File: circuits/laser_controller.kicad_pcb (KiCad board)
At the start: 4 copper layers, 173 x 61.1 mm, 181 parts, among them J1 USB_MINI_B, J2 USB_MINI_B, J5 24V DC IN, J6 CONN_RJ45, J7 C192300, Q1 SOT-23, Q2 SOT-23, Q3 SOT-23, Q4 SOT-23, Q5 SOT-23, Q6 SOT-23, SW1 SW_PUSH, SW2 SW_PUSH, SW3 SW_PUSH, U1 SOIC-8_3.9x4.9mm_P1.27mm, U10 QFN-28-1EP_5x5mm_P0.5mm_EP3.3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, U11 SOT-23-5, U12 TSSOP-14_4.4x5mm_P0.65mm, U13 SOT-23, U14 LQFP-64_10x10mm_P0.5mm, U15 TSOT-23-6, U16 TSOT-23-6, U2 SOIC-8_3.9x4.9mm_P1.27mm, U3 SOIC-8_3.9x4.9mm_P1.27mm, U4 SOIC-8_3.9x4.9mm_P1.27mm, U5 SOT-23-5, U6 SOT-23-5, U7 SOT-23-5, U8 SOT-23-5, U9 ESP32-S3-WROOM-1

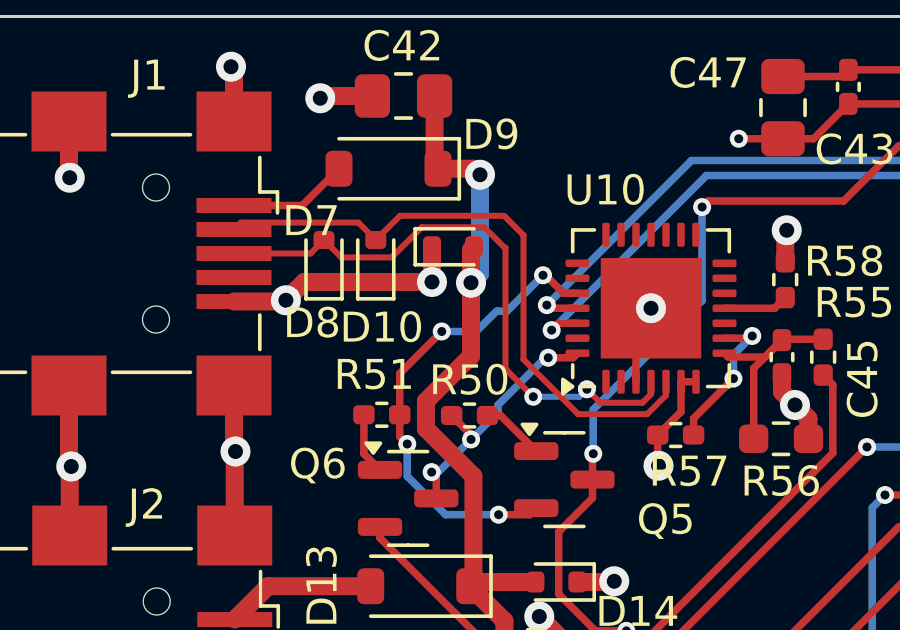
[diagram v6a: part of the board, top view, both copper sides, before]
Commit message: Fix USB PCB routing policy
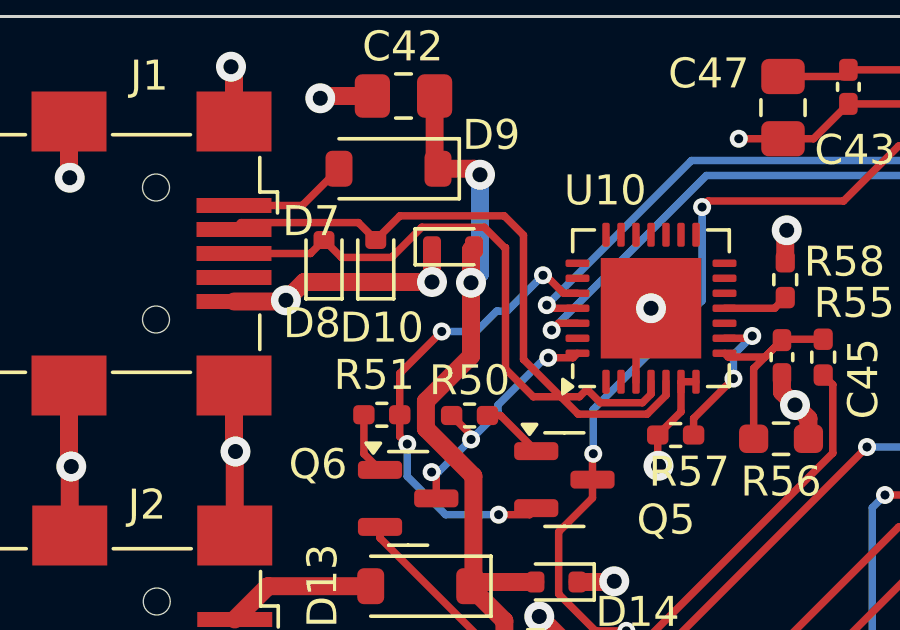
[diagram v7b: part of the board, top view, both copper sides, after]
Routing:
- net /MCU_ESP32-S3/D+: vias 2 -> 0
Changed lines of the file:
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@@
   (segment (start 189.4465 84.434) (end 189.4465 85.962) (width 0.5) (layer "F.Cu") (net 10))
   (segment (start 191.7355 84.434) (end 189.4465 84.434) (width 0.5) (layer "F.Cu") (net 10))
-  (segment (start 51.7389 92.3) (end 52.1889 92.75) (width 0.2) (layer "F.Cu") (net 11))
-  (segment (start 43.555 87.905) (end 45.229448 87.905) (width 0.2) (layer "F.Cu") (net 11))
-  (segment (start 42.975 87.325) (end 43.555 87.905) (width 0.2) (layer "F.Cu") (net 11))
-  (segment (start 49.025 87.580132) (end 49.025 91.625) (width 0.2) (layer "F.Cu") (net 11))
-  (segment (start 45.229448 87.905) (end 46.234448 86.9) (width 0.2) (layer "F.Cu") (net 11))
-  (segment (start 53.875 92.464386) (end 53.875 92.05) (width 0.2) (layer "F.Cu") (net 11))
-  (segment (start 48.995684 87.580132) (end 49.025 87.580132) (width 0.2) (layer "F.Cu") (net 11))
-  (segment (start 49.025 91.625) (end 49.95 92.55) (width 0.2) (layer "F.Cu") (net 11))
-  (segment (start 53.589386 92.75) (end 53.875 92.464386) (width 0.2) (layer "F.Cu") (net 11))
-  (segment (start 39.975 87.775) (end 42.525 87.775) (width 0.2) (layer "F.Cu") (net 11))
-  (segment (start 48.315552 86.9) (end 48.995684 87.580132) (width 0.2) (layer "F.Cu") (net 11))
-  (segment (start 52.1889 92.75) (end 53.589386 92.75) (width 0.2) (layer "F.Cu") (net 11))
-  (segment (start 46.234448 86.9) (end 48.315552 86.9) (width 0.2) (layer "F.Cu") (net 11))
-  (segment (start 42.525 87.775) (end 42.975 87.325) (width 0.2) (layer "F.Cu") (net 11))
-  (via (at 49.95 92.55) (size 0.6) (drill 0.3) (layers "F.Cu" "B.Cu") (net 11))
-  (via (at 51.7389 92.3) (size 0.6) (drill 0.3) (layers "F.Cu" "B.Cu") (net 11))
-  (segment (start 49.95 92.55) (end 51.4889 92.55) (width 0.2) (layer "B.Cu") (net 11))
-  (segment (start 51.4889 92.55) (end 51.7389 92.3) (width 0.2) (layer "B.Cu") (net 11))
-  (segment (start 44.7 87.325) (end 45.505 86.52) (width 0.2) (layer "F.Cu") (net 12))
-  (segment (start 54.375 92.501788) (end 54.375 92.05) (width 0.2) (layer "F.Cu") (net 12))
-  (segment (start 44.12 86.745) (end 44.7 87.325) (width 0.2) (layer "F.Cu") (net 12))
-  (segment (start 51.449239 93.13) (end 53.746788 93.13) (width 0.2) (layer "F.Cu") (net 12))
-  (segment (start 45.505 86.52) (end 48.982151 86.52) (width 0.2) (layer "F.Cu") (net 12))
-  (segment (start 53.746788 93.13) (end 54.375 92.501788) (width 0.2) (layer "F.Cu") (net 12))
-  (segment (start 49.625 87.162849) (end 49.625 91.305761) (width 0.2) (layer "F.Cu") (net 12))
-  (segment (start 49.625 91.305761) (end 51.449239 93.13) (width 0.2) (layer "F.Cu") (net 12))
-  (segment (start 39.975 86.975) (end 40.205 86.745) (width 0.2) (layer "F.Cu") (net 12))
-  (segment (start 40.205 86.745) (end 44.12 86.745) (width 0.2) (layer "F.Cu") (net 12))
-  (segment (start 48.982151 86.52) (end 49.625 87.162849) (width 0.2) (layer "F.Cu") (net 12))
+  (segment (start 51.7389 92.3) (end 52.1889 92.75) (width 0.25) (layer "F.Cu") (net 11))
+  (segment (start 43.555 87.905) (end 45.229448 87.905) (width 0.25) (layer "F.Cu") (net 11))
+  (segment (start 42.975 87.325) (end 43.555 87.905) (width 0.25) (layer "F.Cu") (net 11))
+  (segment (start 49.025 87.580132) (end 49.025 91.625) (width 0.25) (layer "F.Cu") (net 11))
+  (segment (start 45.229448 87.905) (end 46.234448 86.9) (width 0.25) (layer "F.Cu") (net 11))
+  (segment (start 53.875 92.464386) (end 53.875 92.05) (width 0.25) (layer "F.Cu") (net 11))
+  (segment (start 48.995684 87.580132) (end 49.025 87.580132) (width 0.25) (layer "F.Cu") (net 11))
+  (segment (start 49.025 91.625) (end 49.95 92.55) (width 0.25) (layer "F.Cu") (net 11))
+  (segment (start 53.589386 92.75) (end 53.875 92.464386) (width 0.25) (layer "F.Cu") (net 11))
+  (segment (start 39.975 87.775) (end 42.525 87.775) (width 0.25) (layer "F.Cu") (net 11))
+  (segment (start 48.315552 86.9) (end 48.995684 87.580132) (width 0.25) (layer "F.Cu") (net 11))
+  (segment (start 52.1889 92.75) (end 53.589386 92.75) (width 0.25) (layer "F.Cu") (net 11))
+  (segment (start 46.234448 86.9) (end 48.315552 86.9) (width 0.25) (layer "F.Cu") (net 11))
+  (segment (start 42.525 87.775) (end 42.975 87.325) (width 0.25) (layer "F.Cu") (net 11))
+  (segment (start 49.95 92.55) (end 51.4889 92.55) (width 0.25) (layer "F.Cu") (net 11))
+  (segment (start 51.4889 92.55) (end 51.7389 92.3) (width 0.25) (layer "F.Cu") (net 11))
+  (segment (start 44.7 87.325) (end 45.505 86.52) (width 0.25) (layer "F.Cu") (net 12))
+  (segment (start 54.375 92.501788) (end 54.375 92.05) (width 0.25) (layer "F.Cu") (net 12))
+  (segment (start 44.12 86.745) (end 44.7 87.325) (width 0.25) (layer "F.Cu") (net 12))
+  (segment (start 51.449239 93.13) (end 53.746788 93.13) (width 0.25) (layer "F.Cu") (net 12))
+  (segment (start 45.505 86.52) (end 48.982151 86.52) (width 0.25) (layer "F.Cu") (net 12))
+  (segment (start 53.746788 93.13) (end 54.375 92.501788) (width 0.25) (layer "F.Cu") (net 12))
+  (segment (start 49.625 87.162849) (end 49.625 91.305761) (width 0.25) (layer "F.Cu") (net 12))
+  (segment (start 49.625 91.305761) (end 51.449239 93.13) (width 0.25) (layer "F.Cu") (net 12))
+  (segment (start 39.975 86.975) (end 40.205 86.745) (width 0.25) (layer "F.Cu") (net 12))
+  (segment (start 40.205 86.745) (end 44.12 86.745) (width 0.25) (layer "F.Cu") (net 12))
+  (segment (start 48.982151 86.52) (end 49.625 87.162849) (width 0.25) (layer "F.Cu") (net 12))
   (segment (start 50.45 91.25) (end 51.275 91.25) (width 0.25) (layer "F.Cu") (net 13))
   (segment (start 47.877236 93.822236) (end 47.877236 93.972764) (width 0.25) (layer "F.Cu") (net 13))

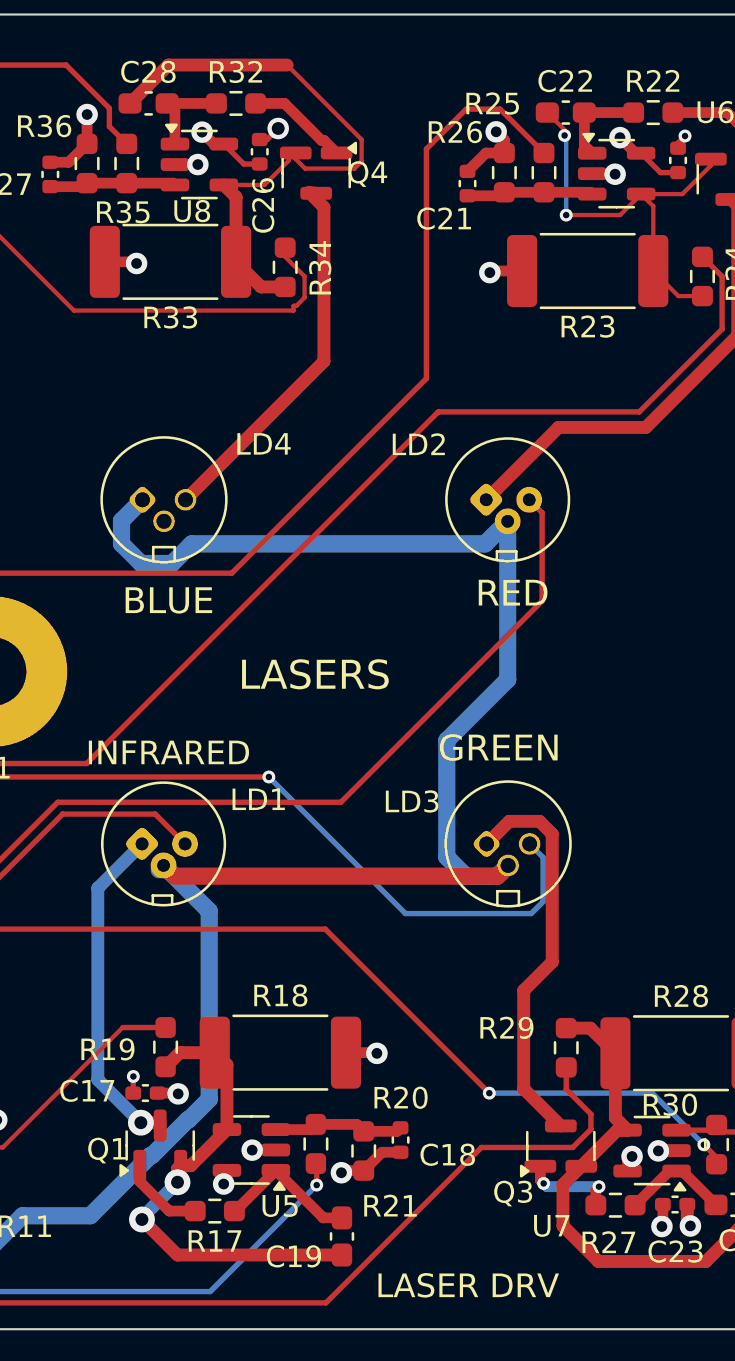
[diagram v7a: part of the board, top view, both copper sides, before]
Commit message: Fix laser control PCB layer vias
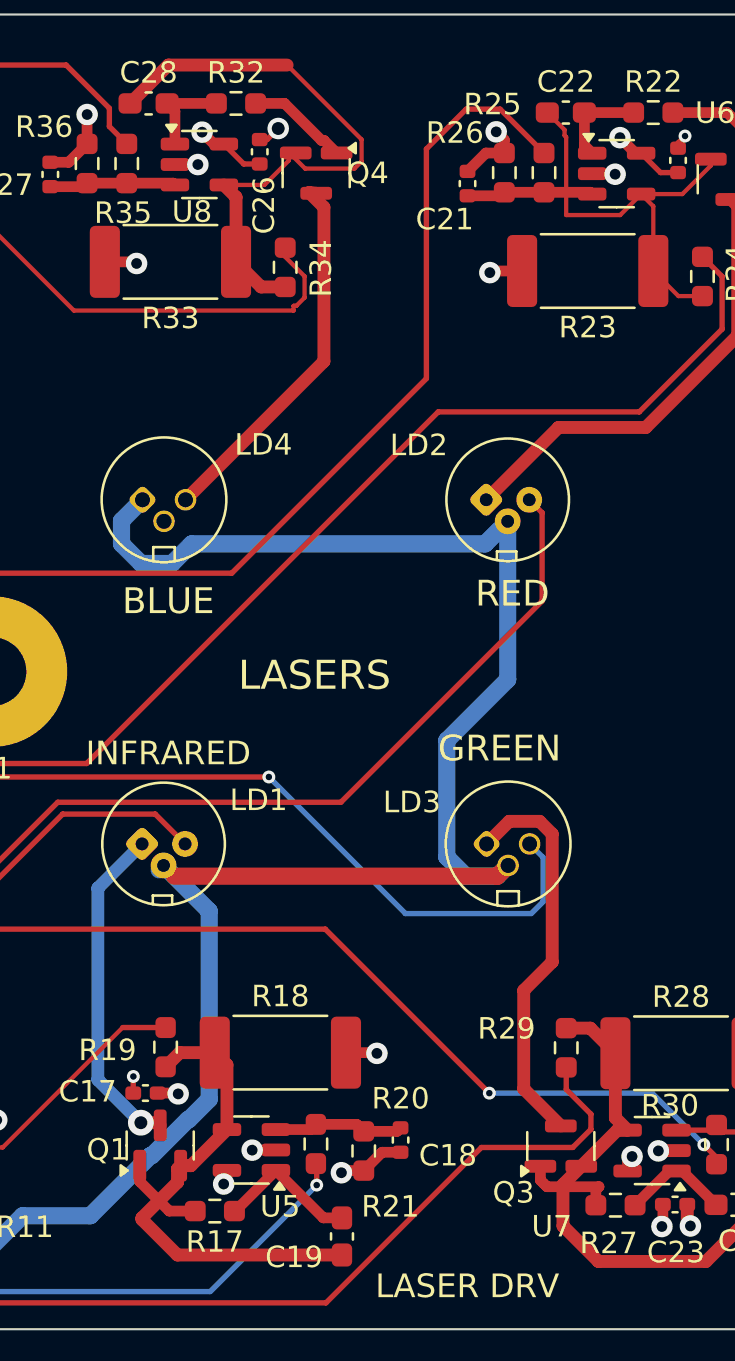
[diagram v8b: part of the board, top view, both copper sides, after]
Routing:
- net Net-(Q3-G): vias 2 -> 0
- net /LASER_RED/FB: vias 2 -> 0
- net /LASER_IR/FB: vias 2 -> 0
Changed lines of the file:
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@@
   (segment (start 170.525 137.55) (end 168.875 135.9) (width 0.6) (layer "F.Cu") (net 7))
   (segment (start 171.148 133.397) (end 172.8275 131.7175) (width 0.6) (layer "F.Cu") (net 7))
-  (via (at 170.52894 134.16832) (size 1.2) (drill 0.6) (layers "F.Cu" "B.Cu") (net 7))
-  (via (at 168.875 135.9) (size 1.2) (drill 0.6) (layers "F.Cu" "B.Cu") (net 7))
-  (segment (start 168.875 135.82226) (end 170.52894 134.16832) (width 0.6) (layer "B.Cu") (net 7))
-  (segment (start 168.875 135.9) (end 168.875 135.82226) (width 0.6) (layer "B.Cu") (net 7))
+  (segment (start 168.875 135.82226) (end 170.52894 134.16832) (width 0.6) (layer "F.Cu") (net 7))
+  (segment (start 168.875 135.9) (end 168.875 135.82226) (width 0.6) (layer "F.Cu") (net 7))
   (segment (start 173.1755 135.5075) (end 173.2125 135.5075) (width 0.5) (layer "F.Cu") (net 8))
   (segment (start 178.175 135.825) (end 177.31 135.825) (width 0.5) (layer "F.Cu") (net 8))
@@
   (segment (start 192.65 91.8) (end 192.65 88.7905) (width 0.2) (layer "F.Cu") (net 9))
   (segment (start 188.525 85.5) (end 188.525 85.2375) (width 0.2) (layer "F.Cu") (net 9))
-  (via (at 188.525 85.5) (size 0.6) (drill 0.3) (layers "F.Cu" "B.Cu") (net 9))
-  (via (at 188.6 89.2) (size 0.6) (drill 0.3) (layers "F.Cu" "B.Cu") (net 9))
-  (segment (start 188.6 85.575) (end 188.525 85.5) (width 0.2) (layer "B.Cu") (net 9))
-  (segment (start 188.6 89.2) (end 188.6 85.575) (width 0.2) (layer "B.Cu") (net 9))
+  (segment (start 188.6 85.575) (end 188.525 85.5) (width 0.2) (layer "F.Cu") (net 9))
+  (segment (start 188.6 89.2) (end 188.6 85.575) (width 0.2) (layer "F.Cu") (net 9))
   (segment (start 189.4465 85.962) (end 189.8085 86.324) (width 0.5) (layer "F.Cu") (net 10))
   (segment (start 189.4465 84.434) (end 189.4465 85.962) (width 0.5) (layer "F.Cu") (net 10))
@@
   (segment (start 189.9775 135.2355) (end 189.9775 134.5225) (width 0.5) (layer "F.Cu") (net 80))
   (segment (start 187.4 133.425) (end 187.4 134.07219) (width 0.5) (layer "F.Cu") (net 80))
-  (via (at 187.551465 134.223655) (size 0.6) (drill 0.3) (layers "F.Cu" "B.Cu") (net 80))
-  (via (at 190.125 134.375) (size 0.6) (drill 0.3) (layers "F.Cu" "B.Cu") (net 80))
-  (segment (start 187.70281 134.375) (end 187.551465 134.223655) (width 0.5) (layer "B.Cu") (net 80))
-  (segment (start 190.125 134.375) (end 187.70281 134.375) (width 0.5) (layer "B.Cu") (net 80))
+  (segment (start 187.70281 134.375) (end 187.551465 134.223655) (width 0.5) (layer "F.Cu") (net 80))
+  (segment (start 190.125 134.375) (end 187.70281 134.375) (width 0.5) (layer "F.Cu") (net 80))
   (segment (start 175.504306 84.009) (end 174.1605 84.009) (width 0.5) (layer "F.Cu") (net 81))
   (segment (start 177.225 85.729694) (end 175.504306 84.009) (width 0.5) (layer "F.Cu") (net 81))
